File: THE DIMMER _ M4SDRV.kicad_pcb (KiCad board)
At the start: 4 copper layers, 37 x 22.3 mm, 81 parts, among them J1 Conn_01x01, J10 GS2, J2 USB_B_Micro, J3 Conn_01x05, J4 Conn_01x02, J5 Conn_01x01, J6 Conn_01x01, J7 Conn_01x04, J8 Conn_01x02, J9 Conn_01x04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

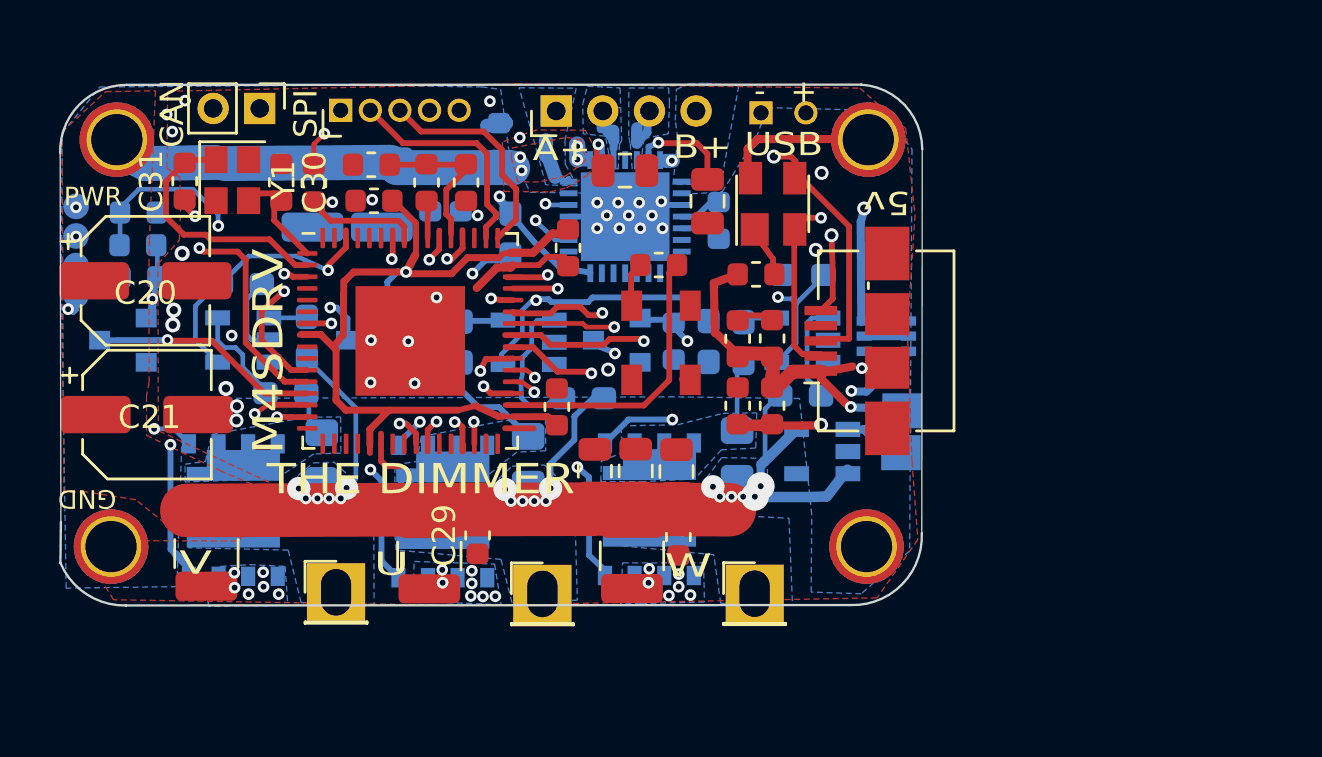
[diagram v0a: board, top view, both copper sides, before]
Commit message: Added curretn sensor and driver
Added current sensor MAX40056 and MOSFET driver MIC4605-2YMT.
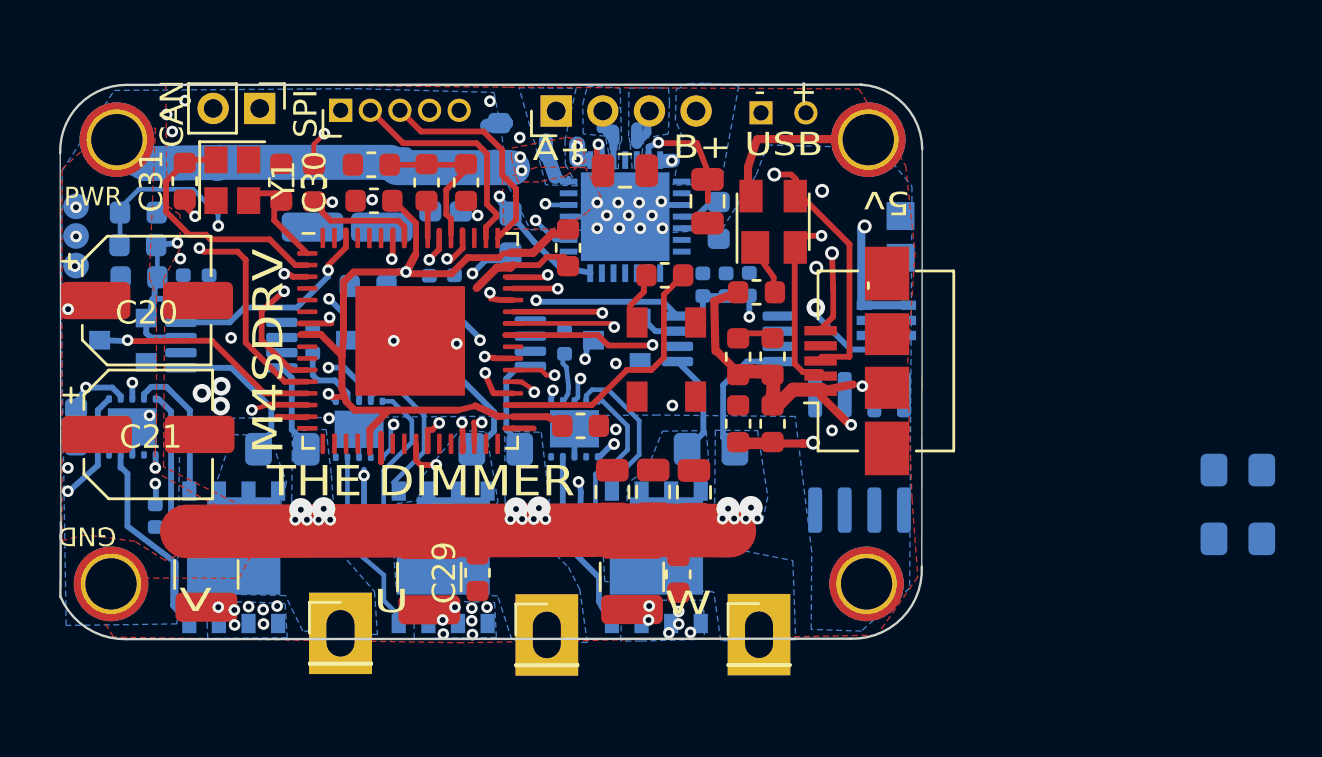
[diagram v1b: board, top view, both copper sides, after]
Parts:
- removed R10, R14, R18: 2k, Resistor_SMD:R_0603_1608Metric_Pad1.05x0.95mm_HandSolder
- removed R11, R13, R15, R17, R7, R9: 100ohm, Resistor_SMD:R_0603_1608Metric_Pad1.05x0.95mm_HandSolder
- added C32: 1uF, Capacitor_SMD:C_0603_1608Metric, B.Cu at (64.2, 72.4)
- added C33: 1uF, Capacitor_SMD:C_0402_1005Metric, B.Cu at (74.4, 68.8)
- added C34: 1uF, Capacitor_SMD:C_0402_1005Metric, B.Cu at (85.2, 68.8)
- added C35: 1uF, Capacitor_SMD:C_0402_1005Metric, B.Cu at (85.8, 76.5)
- added C36: 1uF, Capacitor_SMD:C_0402_1005Metric, B.Cu at (67.6, 76.2)
- added C37: 1uF, Capacitor_SMD:C_0402_1005Metric, B.Cu at (76.6, 76.6)
- added C38: 10nF, Capacitor_SMD:C_0402_1005Metric, B.Cu at (93.1, 66.3)
- added C39: 1uF, Capacitor_SMD:C_0402_1005Metric, B.Cu at (69.9, 66.4)
- added C40: 10nF, Capacitor_SMD:C_0402_1005Metric, B.Cu at (68.8, 66.4)
- added C41: 1uF, Capacitor_SMD:C_0402_1005Metric, B.Cu at (92.1, 66.3)
- added C42: 10nF, Capacitor_SMD:C_0402_1005Metric, B.Cu at (79.4, 66.4)
- added C43: 1uF, Capacitor_SMD:C_0402_1005Metric, B.Cu at (80.4, 66.4)
- added R2: 0.02ohm, Resistor_SMD:R_0805_2012Metric_Pad1.15x1.40mm_HandSolder, B.Cu at (114.0, 77.2)
- added R3: 0.02ohm, Resistor_SMD:R_0805_2012Metric_Pad1.15x1.40mm_HandSolder, B.Cu at (114.0, 74.3)
- added U15: MIC4605-2YMT, LED_SMD:MIC4605, B.Cu at (66.6, 72.4)
- added U16: MIC4605-2YMT, LED_SMD:MIC4605, B.Cu at (76.3, 72.5)
- added U2: MIC4605-2YMT, LED_SMD:MIC4605, B.Cu at (85.6, 72.5)
- C12: footprint Capacitor_SMD:C_0603_1608Metric -> Capacitor_SMD:C_0402_1005Metric
- U12, U13, U7: value Si8540 -> MAX40056_uMAX8; footprint Package_TO_SOT_SMD:SOT-23-5 -> eec:MAX40056F
- U3: value ST730M50R -> LM2672M-12; footprint Package_TO_SOT_SMD:SOT-23-5 -> Package_SO:SOIC-8_3.9x4.9mm_P1.27mm
- moved C14 3.43 mm to (76.7, 66.4), turned to 180 degrees
- moved U12 3.21 mm to (92.1, 68.6), turned to 0 degrees
- moved C12 2.73 mm to (91.1, 66.3), turned to 90 degrees
- moved U13 2.10 mm to (81.5, 68.8), turned to 0 degrees
- moved U4 2.08 mm to (90.7, 80.3)
- moved U5 2.03 mm to (72.6, 80.3)
- moved U6 1.96 mm to (81.6, 80.3)
- moved J6 1.77 mm to (84.4, 81.3)
- moved J5 1.77 mm to (75.5, 81.3)
- moved J1 1.77 mm to (93.5, 81.3)
- moved R12 1.72 mm to (73.1, 73.4), turned to 180 degrees
- moved U3 1.60 mm to (97.8, 73.5), turned to 90 degrees
- moved C28 1.60 mm to (90.0, 78.7)
- moved C29 1.60 mm to (81.4, 78.7)
- moved H3 1.60 mm to (65.7, 79.1)
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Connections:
- J10 pad 1: Net-(J10-Pad1) -> +12V
- U12 pad 1: Net-(R11-Pad2) -> +12V
- U12 pad 2: GND -> Net-(U12-Pad2)
- U12 pad 3: Net-(U12-Pad3) -> +3V3
- U12 pad 4: A3 -> A2
- U12 pad 5: Net-(R13-Pad2) -> (no net)
- U13 pad 1: Net-(R15-Pad2) -> +12V
- U13 pad 2: GND -> Net-(U13-Pad2)
- U13 pad 3: Net-(U13-Pad3) -> +3V3
- U13 pad 4: A2 -> A3
- U13 pad 5: Net-(R17-Pad2) -> (no net)
- U3 pad 1: Net-(J10-Pad1) -> +12V
- U3 pad 2: GND -> Net-(U3-Pad2)
- U3 pad 3: +12V -> Net-(U3-Pad3)
- U3 pad 5: +12V -> Net-(U3-Pad5)
- U4 pad 1: TCC0_CH1/Switch 2 -> HB1_HO
- U4 pad 8: TCC0_CH0/Switch 1 -> HB1_LO
- U5 pad 1: TCC0_CH3/Switch 4 -> HB2_HO
- U5 pad 8: TCC0_CH2/Switch 3 -> HB2_LO
- U6 pad 1: TCC0_CH5/Switch 6 -> HB3_HO
- U6 pad 8: TCC0_CH4/Switch 5 -> HB3_LO
- U7 pad 1: Net-(R7-Pad2) -> +12V
- U7 pad 2: GND -> Net-(U7-Pad2)
- U7 pad 3: Net-(U7-Pad3) -> +3V3
- U7 pad 5: Net-(R9-Pad2) -> (no net)
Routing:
- net TCC0_CH2/Switch 3: track 36.9 -> 3.94 mm, vias 2 -> 1
- net +3V3: track 63.8 -> 88.0 mm, vias 8 -> 11
- net TCC0_CH4/Switch 5: track 20.3 -> 0.00 mm, vias 2 -> 0
- net A5: track 19.8 -> 2.04 mm, vias 2 -> 1
- net A3: track 46.3 -> 34.2 mm
- net U: track 0.00 -> 11.9 mm
- net W: track 0.00 -> 10.8 mm
- net V: track 0.00 -> 9.62 mm
- net Net-(C37-Pad1): track 0.00 -> 9.49 mm, vias 0 -> 2
- net HB2_LO: track 0.00 -> 8.60 mm
- net HB1_LO: track 0.00 -> 7.85 mm
- net HB3_LO: track 0.00 -> 7.72 mm
- net Net-(C36-Pad1): track 0.00 -> 7.03 mm, vias 0 -> 2
- net Net-(C35-Pad1): track 0.00 -> 6.69 mm, vias 0 -> 2
- net HB3_HO: track 0.00 -> 6.56 mm
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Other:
- board size 37 x 22.3 mm -> 37 x 23.8 mm

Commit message: update
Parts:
- removed C10, C9: 10uF, Capacitor_SMD:C_1210_3225Metric
- removed C24: 10nF, Capacitor_SMD:C_0603_1608Metric
- removed J10: GS2, LED_SMD:Solder joint
- removed R12, R16: 0.02ohm, Resistor_SMD:R_0805_2012Metric_Pad1.15x1.40mm_HandSolder
- added C22: 1uF7, Capacitor_SMD:C_0603_1608Metric, F.Cu at (94.0, 75.0)
- added C25: 4.7uF, Capacitor_SMD:C_0805_2012Metric, F.Cu at (99.5, 75.1)
- added C28: 1uF, Capacitor_SMD:C_0603_1608Metric, F.Cu at (99.5, 78.3)
- added C44: 1uF, Capacitor_SMD:C_0402_1005Metric, B.Cu at (96.0, 68.9)
- added C45: 1uF, Capacitor_SMD:C_0402_1005Metric, B.Cu at (94.8, 76.5)
- added C8: 10uF, Capacitor_SMD:C_1210_3225Metric, F.Cu at (97.6, 78.7)
- added J11: Conn_01x01, Connector_PinHeader_2.54mm:PinHeader_1x01_P2.54mm_Vertical, F.Cu at (102.5, 81.6)
- added J12: Conn_01x02, Connector_PinHeader_2.00mm:PinHeader_1x02_P2.00mm_Vertical, F.Cu at (100.4, 59.2)
- added U17: MIC4605-2YMT, LED_SMD:MIC4605, B.Cu at (94.8, 72.5)
- added U18: BSC0925NDATMA1, Package_SON:Infineon_PG-TISON-8-2, B.Cu at (99.7, 80.3)
- C11, C16, C19, C2: footprint Capacitor_SMD:C_0603_1608Metric -> Capacitor_SMD:C_0402_1005Metric
- C22, C23, U8: moved to F.Cu
- J2: footprint Connector_USB:USB_Micro-B_Amphenol_10104110_Horizontal -> molex_usb_vert:MOLEX_1051330001
- J3: footprint Connector_PinHeader_1.27mm:PinHeader_1x05_P1.27mm_Vertical -> Connector_PinHeader_2.54mm:PinHeader_1x04_P2.54mm_Vertical
- J4: footprint Connector_PinHeader_2.00mm:PinHeader_1x02_P2.00mm_Vertical -> Connector_PinSocket_2.54mm:PinSocket_1x02_P2.54mm_Vertical
- J7: footprint Connector_PinHeader_2.00mm:PinHeader_1x04_P2.00mm_Vertical -> Connector_PinHeader_2.54mm:PinHeader_1x04_P2.54mm_Vertical
- J8: footprint Connector_PinHeader_1.27mm:PinHeader_1x02_P1.27mm_Vertical -> Connector_PinHeader_2.00mm:PinHeader_1x02_P2.00mm_Vertical
- L1: footprint Inductor_SMD:L_0603_1608Metric -> Inductor_SMD:L_0402_1005Metric
- R6: footprint Resistor_SMD:R_0603_1608Metric -> Resistor_SMD:R_0402_1005Metric
- moved R2 38.9 mm to (75.2, 78.7)
- moved R3 30.1 mm to (84.3, 78.7)
- moved C23 21.8 mm to (97.3, 74.8), turned to -90 degrees
- moved J7 21.6 mm to (105.4, 65.6), turned to 0 degrees
- moved C22 19.9 mm to (95.9, 74.8)
- moved R21 17.0 mm to (99.9, 64.8), turned to 0 degrees
- moved R19 16.1 mm to (103.2, 73.5)
- moved R20 15.8 mm to (103.0, 65.4), turned to -90 degrees
- moved U14 14.4 mm to (100.9, 69.4), turned to 90 degrees
- moved J9 13.1 mm to (77.0, 62.4), turned to 0 degrees
- moved C19 12.9 mm to (100.6, 73.0), turned to 180 degrees
- moved R8 12.5 mm to (93.5, 78.8)
- moved J2 11.4 mm to (89.2, 61.9), turned to 180 degrees
- moved U3 10.1 mm to (98.2, 63.4), turned to 180 degrees
- moved U8 9.13 mm to (90.2, 65.2), turned to 0 degrees
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- renumbered U7 to U12, U12 to U7
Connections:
- net TCC0_CH2/Switch 3 renamed TCC0_CH2/CAN0Switch 3
- R2 pad 1: +12V -> V
- R2 pad 2: +12V -> V
- R3 pad 1: +12V -> U
- R3 pad 2: +12V -> U
- R8 pad 1: +12V -> W
- R8 pad 2: +12V -> W
- U1 pad 25: CAN1_TX -> Net-(U1-Pad25)
- U1 pad 26: CAN1_RX -> CAN1_STANDBY
- U1 pad 27: Net-(U1-Pad27) -> CAN1_TX
- U1 pad 28: Net-(U1-Pad28) -> CAN1_RX
- U12 pad 1: +12V -> V
- U12 pad 8: +12V -> V
- U13 pad 1: +12V -> U
- U13 pad 8: +12V -> U
- U15 pad 11: GND -> (no net)
- U16 pad 11: GND -> (no net)
- U2 pad 11: GND -> (no net)
- U7 pad 1: +12V -> W
- U7 pad 8: +12V -> W
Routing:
- net +12V: track 80.0 -> 44.6 mm, vias 24 -> 29
- net UART_TX: track 11.8 -> 35.4 mm
- net V: track 9.62 -> 31.6 mm
- net W: track 10.8 -> 32.2 mm
- net U: track 11.9 -> 33.3 mm
- net VBUS: track 30.8 -> 12.8 mm, vias 2 -> 0
- net UART_RX: track 17.4 -> 33.0 mm
- net GND: track 31.2 -> 16.8 mm, vias 56 -> 65
- net Net-(C45-Pad1): track 0.00 -> 12.3 mm, vias 0 -> 2
- net X: track 0.00 -> 11.5 mm
- net SWDIO: track 17.1 -> 5.67 mm, vias 2 -> 1
- net SWCLK: track 19.3 -> 8.90 mm, vias 2 -> 1
- net D+: track 28.7 -> 18.8 mm, vias 2 -> 1
- net A3: track 34.2 -> 25.2 mm
- net STEP: track 11.5 -> 20.5 mm
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- added copper zone on B.Cu, net X
- removed copper zone on In1.Cu, net +12V
- removed copper zone on In2.Cu, net +12V
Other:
- board size 37 x 23.8 mm -> 43.1 x 23.2 mm
- board text added: "CLK"
- board text added: "COM"
- board text added: "DIO"
- board text added: "RX"
- board text added: "TX"
- board text added: "X"
- board text removed: "-"
- board text removed: "SPI"

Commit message: Dev.
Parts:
- removed the C8 at (97.6, 78.7)
- added C10: 10uF, Capacitor_SMD:C_1210_3225Metric, F.Cu at (97.9, 78.2)
- added C24: 10nF, Capacitor_SMD:C_0603_1608Metric, F.Cu at (92.2, 77.7)
- added C46: 2.2uF, Capacitor_SMD:C_0603_1608Metric, B.Cu at (98.6, 62.0)
- added C47: 200nF, Capacitor_SMD:C_0603_1608Metric, B.Cu at (100.1, 62.0)
- added C49: 0.1uF, Capacitor_SMD:C_0603_1608Metric, B.Cu at (93.6, 63.3)
- added C50: 200nF, Capacitor_SMD:C_0603_1608Metric, B.Cu at (87.1, 65.4)
- added C51: 200nF, Capacitor_SMD:C_0603_1608Metric, B.Cu at (82.9, 60.2)
- added J10: GS2, Resistor_SMD:R_0805_2012Metric, B.Cu at (85.8, 57.5)
- added J8: Conn_01x02, Connector_PinHeader_2.00mm:PinHeader_1x02_P2.00mm_Vertical, F.Cu at (90.1, 57.6)
- added L2: 33uH, Inductor_SMD:L_Coilcraft_XxL4020, B.Cu at (84.1, 64.4)
- added R1: 100k, Resistor_SMD:R_0603_1608Metric, B.Cu at (95.9, 59.6)
- added R7: 11.11k, Resistor_SMD:R_0603_1608Metric, B.Cu at (95.9, 61.0)
- added U19: MCP2562FD-E_SN, Package_DFN_QFN:DFN-8-1EP_3x3mm_P0.65mm_EP1.55x2.4mm, B.Cu at (70.2, 64.4)
- added U20: LF15_TO220, Package_TO_SOT_SMD:SOT-23-5, F.Cu at (65.5, 63.0)
- C1, C13, C30, C31: footprint Capacitor_SMD:C_0603_1608Metric -> Capacitor_SMD:C_0402_1005Metric
- R5: footprint Resistor_SMD:R_0603_1608Metric -> Resistor_SMD:R_0402_1005Metric
- U10: value DRV50153A -> DRV5053
- U11, U9: value DRV50152A -> DRV5053
- U3: value LM2672M-12 -> LMR50410; footprint Package_SO:SOIC-8_3.9x4.9mm_P1.27mm -> Package_TO_SOT_SMD:SOT-23-6
- U8: value NCP170 -> MIC5219-3.6; footprint Package_TO_SOT_SMD:SOT-363_SC-70-6 -> Package_TO_SOT_SMD:SOT-23-5
- moved C25 23.9 mm to (75.8, 78.4), turned to 90 degrees
- moved H3 21.1 mm to (65.5, 58.4)
- moved C23 20.3 mm to (77.3, 78.6), turned to 90 degrees
- moved C22 20.0 mm to (74.3, 78.6), turned to 90 degrees
- moved H2 19.8 mm to (65.5, 80.3)
- moved C26 8.14 mm to (100.2, 77.9), turned to 90 degrees
- moved C28 7.02 mm to (83.0, 78.3)
- moved C25 6.81 mm to (84.6, 78.1), turned to 90 degrees
- moved C27 5.35 mm to (93.7, 77.6), turned to 90 degrees
- moved C28 4.75 mm to (101.7, 74.1), turned to 0 degrees
- moved C29 4.67 mm to (86.1, 78.3)
- moved C44 4.66 mm to (92.9, 72.4), turned to -90 degrees
- moved C43 4.06 mm to (78.6, 62.7), turned to 180 degrees
- moved C33 3.28 mm to (74.2, 72.0), turned to -90 degrees
- moved J4 3.10 mm to (69.9, 57.5), turned to 90 degrees
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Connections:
- C18 pad 2: +12V -> VIN
- C20 pad 1: +12V -> VIN
- C21 pad 1: +12V -> VIN
- C22 pad 2: +12V -> VIN (x2)
- C23 pad 2: +12V -> VIN
- C25 pad 2: +12V -> VIN (x2)
- C26 pad 2: +12V -> VIN
- C27 pad 2: +12V -> VIN
- C28 pad 2: +12V -> VIN (x2)
- C29 pad 2: +12V -> VIN
- C32 pad 1: +12V -> VOUT/10v
- C33 pad 1: +12V -> VOUT/10v
- C34 pad 1: +12V -> VOUT/10v
- C44 pad 1: +12V -> VOUT/10v
- C7 pad 2: +12V -> VIN
- C8 pad 2: +12V -> VIN
- H2 pad 1: +12V -> VIN
- J4 pad 1: CAN1_RX -> CAN_L
- J4 pad 2: CAN1_TX -> CAN_H
- U14 pad 22: +12V -> VIN
- U14 pad 28: +12V -> VIN
- U15 pad 2: +12V -> VOUT/10v
- U16 pad 2: +12V -> VOUT/10v
- U17 pad 2: +12V -> VOUT/10v
- U18 pad 2: +12V -> VIN
- U2 pad 2: +12V -> VOUT/10v
- U3 pad 1: +12V -> Net-(C49-Pad2)
- U3 pad 2: Net-(U3-Pad2) -> GND
- U3 pad 4: Net-(U3-Pad4) -> VIN
- U3 pad 5: Net-(U3-Pad5) -> VIN
- U3 pad 6: GND -> Net-(C49-Pad1)
- U4 pad 2: +12V -> VIN
- U5 pad 2: +12V -> VIN
- U6 pad 2: +12V -> VIN
- U8 pad 3: +3V3 -> /+5v_filtered
- U8 pad 4: (no net) -> Net-(U8-Pad4)
- U8 pad 5: GND -> +3V3
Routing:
- net VOUT/10v: track 0.00 -> 69.9 mm, vias 0 -> 5
- net VIN: track 0.00 -> 62.3 mm, vias 0 -> 31
- net +12V: track 44.6 -> 0.00 mm, vias 29 -> 0
- net VBUS: track 12.8 -> 35.0 mm, vias 0 -> 3
- net A5: track 2.04 -> 23.9 mm, vias 1 -> 2
- net Net-(C49-Pad1): track 0.00 -> 18.5 mm
- net D+: track 18.8 -> 26.7 mm
- net CAN_H: track 0.00 -> 6.14 mm
- net CAN_L: track 0.00 -> 5.38 mm
- net Net-(C36-Pad1): track 7.03 -> 12.1 mm
- net A3: track 25.2 -> 21.4 mm
- net Net-(R20-Pad2): track 0.00 -> 3.57 mm, vias 0 -> 1
- net +3V3: track 95.2 -> 98.5 mm, vias 10 -> 11
- net Net-(R1-Pad2): track 0.00 -> 3.31 mm
- net Net-(R19-Pad2): track 0.00 -> 3.26 mm, vias 0 -> 1
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- added copper zone on B.Cu, net VIN
- added copper zone on F.Cu, net VIN
- removed copper zone on B.Cu, net +12V
- removed copper zone on F.Cu, net +12V
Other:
- board size 43.1 x 23.2 mm -> 43.1 x 26.2 mm
- board text added: "3V3"
- board text added: "3v"
- board text added: "A-"
- board text added: "A0"
- board text added: "A0/DAC"
- board text added: "B-"
- board text added: "Bridge"
- board text added: "CK"
- board text added: "H"
- board text added: "L"
- board text added: "M4SDRV µ"
- board text added: "MI"
- board text added: "MISO"
- board text added: "MO"
- board text added: "MOSI"
- board text added: "SCK"
- board text added: "VIN"
- board text added: "YXZXCX"
- board text removed: "B+"
- board text removed: "M4SDRV"
- board text removed: "PWR"
- board text removed: "SWO"
- board text removed: "THE DIMMER"
- board text removed: "USB"
